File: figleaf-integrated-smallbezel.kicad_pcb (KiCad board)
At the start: 2 copper layers, 145 x 106 mm, 70 parts, among them J1 Conn_01x02_Pin, J2 HRO_TYPE-C-31-M-14, J3 Battery, J9 TC2030_SWD, Q2 2N7002, SW1 PWR, SW2 RST, U1 SRV05-4, U10 MAX17048, U3 BQ24075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

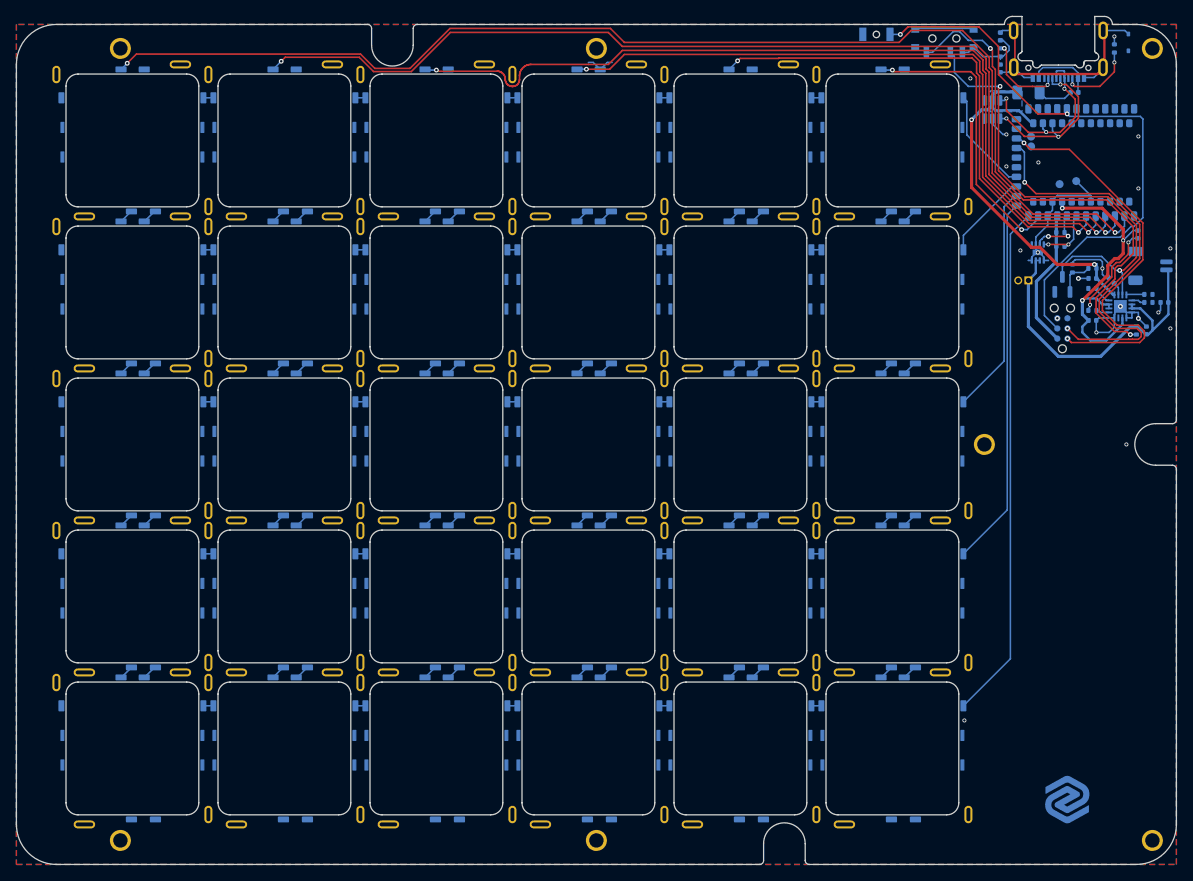
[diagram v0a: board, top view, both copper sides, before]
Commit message: Add thin bezel test + move front IO checkpoint
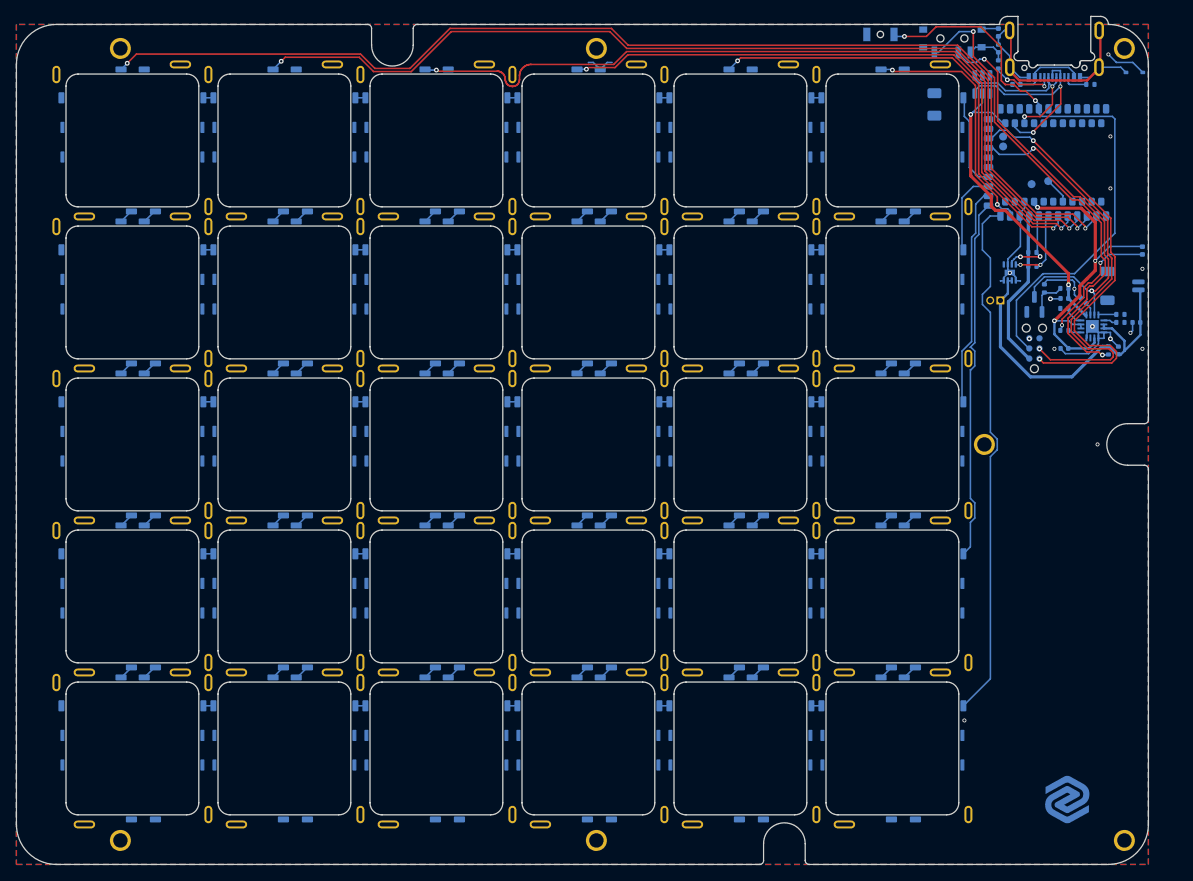
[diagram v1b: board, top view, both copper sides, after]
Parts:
- moved F1 11.8 mm to (127.2, 22.5), turned to -90 degrees
- moved L1 7.32 mm to (137.5, 20.0)
- moved R1 5.41 mm to (146.8, 20.0), turned to 180 degrees
- moved C6 4.95 mm to (143.5, 53.0), turned to 180 degrees
- moved C17 4.30 mm to (150.2, 53.2)
- moved C5 4.30 mm to (143.5, 46.8)
- moved C7 4.30 mm to (152.5, 49.8)
- moved J1 4.30 mm to (135.5, 47.0)
- moved J3 4.30 mm to (150.8, 45.2)
- moved J9 4.30 mm to (139.8, 53.0)
- moved Q2 4.30 mm to (139.8, 47.5)
- moved R10 4.30 mm to (143.5, 50.8)
- moved R11 4.30 mm to (145.9, 47.0)
- moved R12 4.30 mm to (143.5, 48.0)
- moved R13 4.30 mm to (150.5, 48.8)
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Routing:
- net GND_L: track 70.0 -> 57.7 mm, vias 20 -> 15
- net col_0: track 151.1 -> 143.7 mm
- net +5V: track 47.5 -> 40.2 mm
- net Net-(J2-CC2): track 9.39 -> 3.04 mm, vias 2 -> 0
- net col_1: track 129.3 -> 122.9 mm
- net col_3: track 84.7 -> 78.8 mm
- net SYSOFF: track 59.5 -> 54.0 mm
- net Net-(SW1-A): track 64.8 -> 59.3 mm
- net col_4: track 64.3 -> 59.0 mm
- net col_2: track 108.1 -> 102.9 mm
- net col_5: track 36.7 -> 31.5 mm
- net Net-(F1-Pad1): track 4.49 -> 0.00 mm
- net Net-(LED2-K): track 12.0 -> 16.3 mm
- net USB-D+: track 22.4 -> 26.4 mm, vias 3 -> 2
- net SWDIO: track 50.4 -> 53.9 mm
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- removed copper zone on B.Cu, net +5V
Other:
- board size 145 x 106 mm -> 141.5 x 106 mm
